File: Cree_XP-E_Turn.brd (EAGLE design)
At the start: 32 x 20 mm, 5 parts

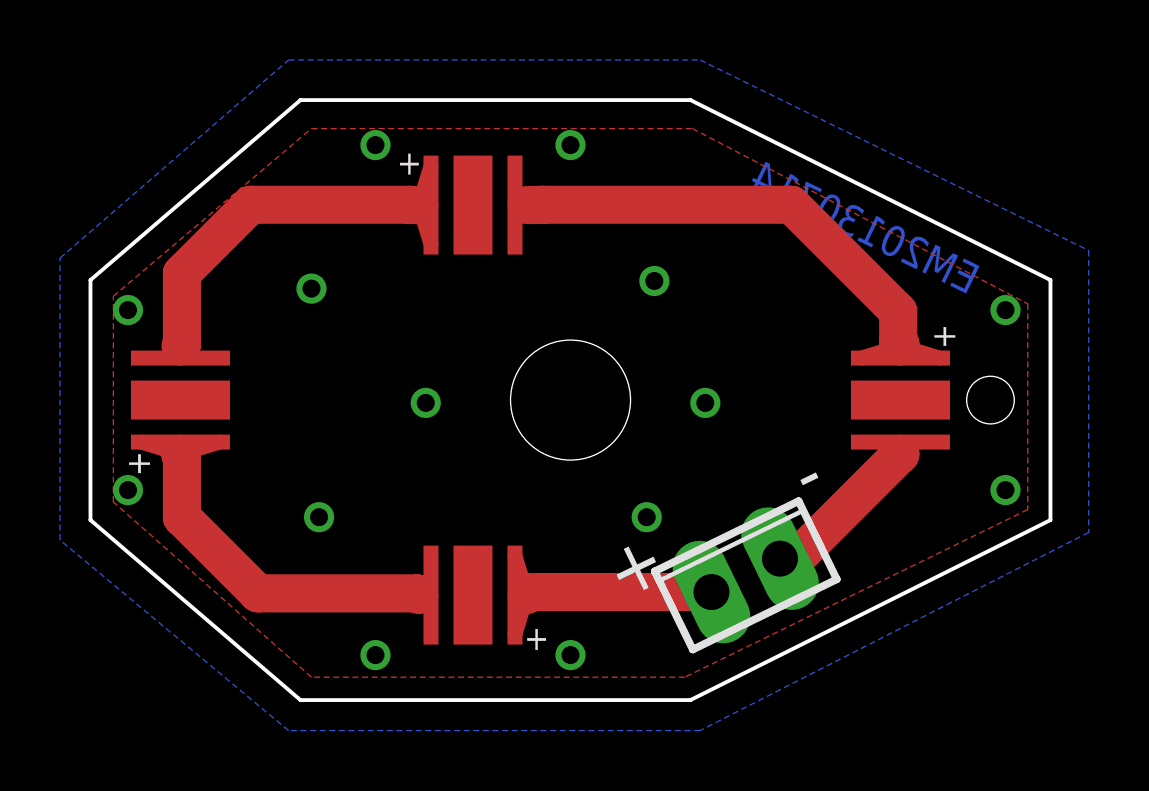
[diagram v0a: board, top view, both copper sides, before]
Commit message: Used Updated XP-E footprint
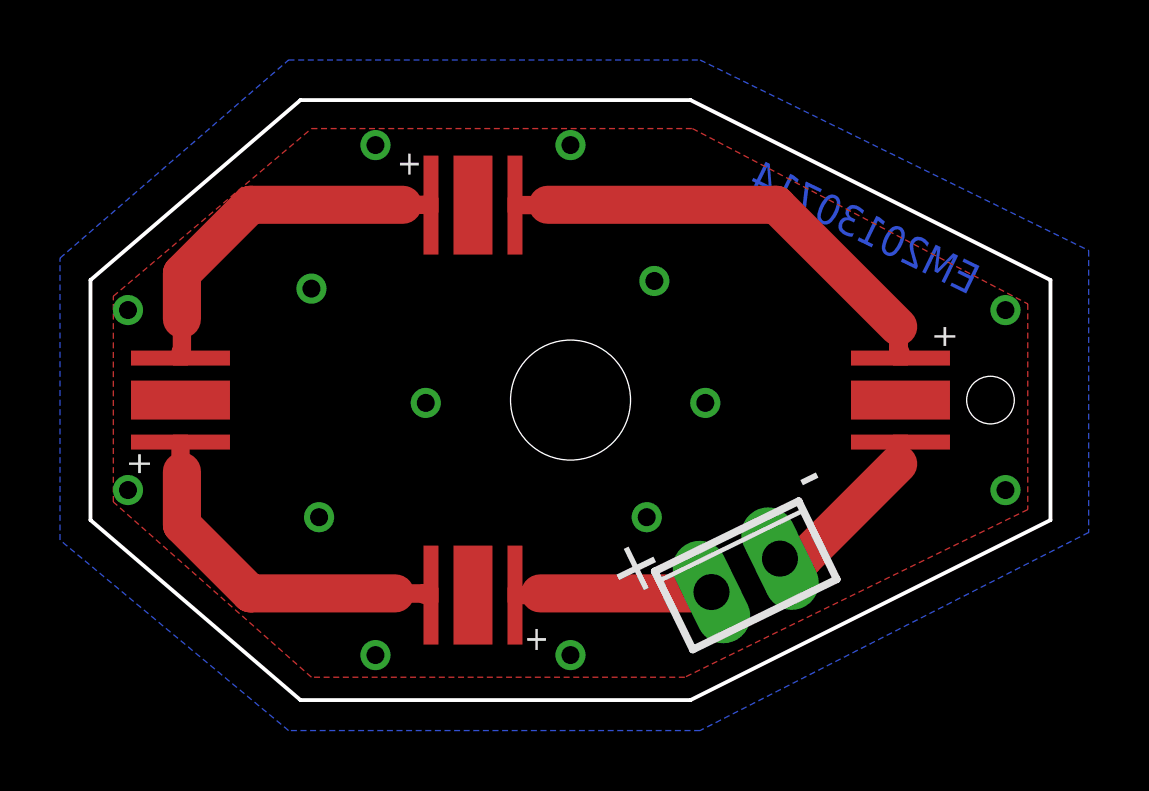
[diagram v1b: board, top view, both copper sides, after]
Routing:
- net N$4: track 11.1 -> 11.6 mm
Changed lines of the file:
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@@
 <setting verticaltext="up"/>
 </settings>
-<grid distance="0.254" unitdist="mm" unit="mm" style="lines" multiple="1" display="no" altdistance="0.025" altunitdist="inch" altunit="inch"/>
+<grid distance="0.254" unitdist="mm" unit="inch" style="lines" multiple="1" display="no" altdistance="0.025" altunitdist="inch" altunit="inch"/>
 <layers>
 <layer number="1" name="Top" color="4" fill="1" visible="yes" active="yes"/>
@@
 <contactref element="X1" pad="2"/>
 <contactref element="LED1" pad="CT"/>
-<wire x1="22.983465625" y1="4.71473125" x2="23.51073125" y2="4.71473125" width="1.27" layer="1"/>
-<wire x1="23.51073125" y1="4.71473125" x2="26.996" y2="8.2" width="1.27" layer="1"/>
-<wire x1="27" y1="8.2" x2="26.996" y2="8.2" width="1.27" layer="1"/>
+<wire x1="27" y1="8.4" x2="26.924" y2="8.324" width="0.6096" layer="1"/>
+<wire x1="26.924" y1="8.324" x2="26.924" y2="7.874" width="0.6096" layer="1"/>
+<wire x1="26.924" y1="7.874" x2="23.76473125" y2="4.71473125" width="1.27" layer="1"/>
+<wire x1="23.76473125" y1="4.71473125" x2="22.983465625" y2="4.71473125" width="1.27" layer="1"/>
 </signal>
 <signal name="N$2">
 <contactref element="LED1" pad="AN"/>
 <contactref element="LED2" pad="CT"/>
-<wire x1="14.55" y1="16.5" x2="15.068" y2="16.51" width="1.27" layer="1"/>
-<wire x1="15.068" y1="16.51" x2="23.368" y2="16.51" width="1.27" layer="1"/>
-<wire x1="23.368" y1="16.51" x2="26.924" y2="12.954" width="1.27" layer="1"/>
-<wire x1="26.924" y1="12.954" x2="26.924" y2="11.938" width="1.27" layer="1"/>
-<wire x1="27" y1="11.8" x2="27" y2="11.862" width="1.27" layer="1"/>
-<wire x1="27" y1="11.862" x2="26.924" y2="11.938" width="1.27" layer="1"/>
+<wire x1="27" y1="11.6" x2="26.924" y2="11.676" width="0.6096" layer="1"/>
+<wire x1="26.924" y1="11.676" x2="26.924" y2="12.446" width="0.6096" layer="1"/>
+<wire x1="26.924" y1="12.446" x2="22.86" y2="16.51" width="1.27" layer="1"/>
+<wire x1="22.86" y1="16.51" x2="15.24" y2="16.51" width="1.27" layer="1"/>
+<wire x1="15.24" y1="16.51" x2="15.23" y2="16.5" width="0.6096" layer="1"/>
+<wire x1="15.23" y1="16.5" x2="14.35" y2="16.5" width="0.6096" layer="1"/>
 </signal>
 <signal name="N$3">
 <contactref element="LED2" pad="AN"/>
 <contactref element="LED3" pad="CT"/>
-<wire x1="3" y1="11.8" x2="3.048" y2="11.848" width="1.27" layer="1"/>
-<wire x1="3.048" y1="11.848" x2="3.048" y2="14.224" width="1.27" layer="1"/>
-<wire x1="3.048" y1="14.224" x2="5.334" y2="16.51" width="1.27" layer="1"/>
-<wire x1="5.334" y1="16.51" x2="10.668" y2="16.51" width="1.27" layer="1"/>
-<wire x1="10.95" y1="16.5" x2="10.678" y2="16.5" width="1.27" layer="1"/>
-<wire x1="10.678" y1="16.5" x2="10.668" y2="16.51" width="1.27" layer="1"/>
+<wire x1="11.15" y1="16.5" x2="11.14" y2="16.51" width="0.6096" layer="1"/>
+<wire x1="11.14" y1="16.51" x2="10.414" y2="16.51" width="0.6096" layer="1"/>
+<wire x1="10.414" y1="16.51" x2="5.334" y2="16.51" width="1.27" layer="1"/>
+<wire x1="5.334" y1="16.51" x2="3.048" y2="14.224" width="1.27" layer="1"/>
+<wire x1="3.048" y1="14.224" x2="3.048" y2="12.7" width="1.27" layer="1"/>
+<wire x1="3.048" y1="12.7" x2="3.048" y2="11.648" width="0.6096" layer="1"/>
+<wire x1="3.048" y1="11.648" x2="3" y2="11.6" width="0.6096" layer="1"/>
 </signal>
 <signal name="N$4">
 <contactref element="LED3" pad="AN"/>
 <contactref element="LED4" pad="CT"/>
-<wire x1="10.95" y1="3.5" x2="10.894" y2="3.556" width="1.27" layer="1"/>
-<wire x1="10.894" y1="3.556" x2="5.588" y2="3.556" width="1.27" layer="1"/>
-<wire x1="5.588" y1="3.556" x2="3.048" y2="6.096" width="1.27" layer="1"/>
-<wire x1="3.048" y1="6.096" x2="3.048" y2="8.128" width="1.27" layer="1"/>
-<wire x1="3" y1="8.2" x2="3" y2="8.176" width="1.27" layer="1"/>
-<wire x1="3" y1="8.176" x2="3.048" y2="8.128" width="1.27" layer="1"/>
+<wire x1="3" y1="8.4" x2="3" y2="7.668" width="0.6096" layer="1"/>
+<wire x1="3" y1="7.668" x2="3.048" y2="7.62" width="0.6096" layer="1"/>
+<wire x1="3.048" y1="7.62" x2="3.048" y2="5.842" width="1.27" layer="1"/>
+<wire x1="3.048" y1="5.842" x2="5.334" y2="3.556" width="1.27" layer="1"/>
+<wire x1="5.334" y1="3.556" x2="10.16" y2="3.556" width="1.27" layer="1"/>
+<wire x1="10.16" y1="3.556" x2="11.094" y2="3.556" width="0.6096" layer="1"/>
+<wire x1="11.094" y1="3.556" x2="11.15" y2="3.5" width="0.6096" layer="1"/>
 </signal>
 <signal name="V+">
 <contactref element="LED4" pad="AN"/>
 <contactref element="X1" pad="1"/>
-<wire x1="14.55" y1="3.5" x2="14.651265625" y2="3.601265625" width="1.27" layer="1"/>
-<wire x1="14.651265625" y1="3.601265625" x2="20.70053125" y2="3.601265625" width="1.27" layer="1"/>
+<wire x1="14.35" y1="3.5" x2="14.93" y2="3.5" width="0.6096" layer="1"/>
+<wire x1="14.93" y1="3.5" x2="14.986" y2="3.556" width="0.6096" layer="1"/>
+<wire x1="14.986" y1="3.556" x2="20.655265625" y2="3.556" width="1.27" layer="1"/>
+<wire x1="20.655265625" y1="3.556" x2="20.70053125" y2="3.601265625" width="1.27" layer="1"/>
 </signal>
 <signal name="THERMAL">
